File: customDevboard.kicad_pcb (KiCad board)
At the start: 2 copper layers, 39 x 39 mm, 83 parts, among them J1 USB_C_Receptacle_USB2.0_14P, J10 GPIO29_ADC3, J11 GND, J12 GPIO0, J13 GPIO1, J14 GPIO2, J15 GPIO3, J16 GPIO4, J17 GPIO5, J18 GPIO6, J19 GPIO7, J2 RUN, J20 GPIO8, J21 GPIO9, J22 Conn_01x01, J23 Conn_01x01, J24 Conn_01x01, J25 Conn_01x01, J26 Conn_01x01, J27 Conn_01x01, J28 Conn_01x01, J29 Conn_01x01, J3 3V3, J30 Conn_01x01, J31 Conn_01x01, J32 Conn_01x01, J33 Conn_01x01, J34 Conn_01x01, J35 Conn_01x01, J36 Conn_01x01, J37 Conn_01x01, J38 Conn_01x01, J39 Conn_01x01, J4 VBUS, J40 Conn_01x01, J41 Conn_01x01, J42 SWCLK, J43 GND, J44 SWD, J5 GND, J6 GND, J7 GPIO26_ADC0, J8 GPIO27_ADC1, J9 GPIO28_ADC2, SW1 BOOT, U1 RP2040, U2 W25Q128JVP, U3 TLV75733PDRV, Y1 12 MHz

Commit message: optimise more
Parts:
- moved C12 12.2 mm to (69.2, 69.0), turned to -90 degrees
- moved C11 10.8 mm to (70.2, 69.0), turned to -90 degrees
- moved C10 9.65 mm to (71.2, 69.0), turned to -90 degrees
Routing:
- net +1V1: track 39.9 -> 33.2 mm
- net GND: track 30.5 -> 26.5 mm
- net Net-(U1-USB_DM): track 10.5 -> 8.99 mm
- net Net-(U1-USB_DP): track 10.1 -> 8.97 mm

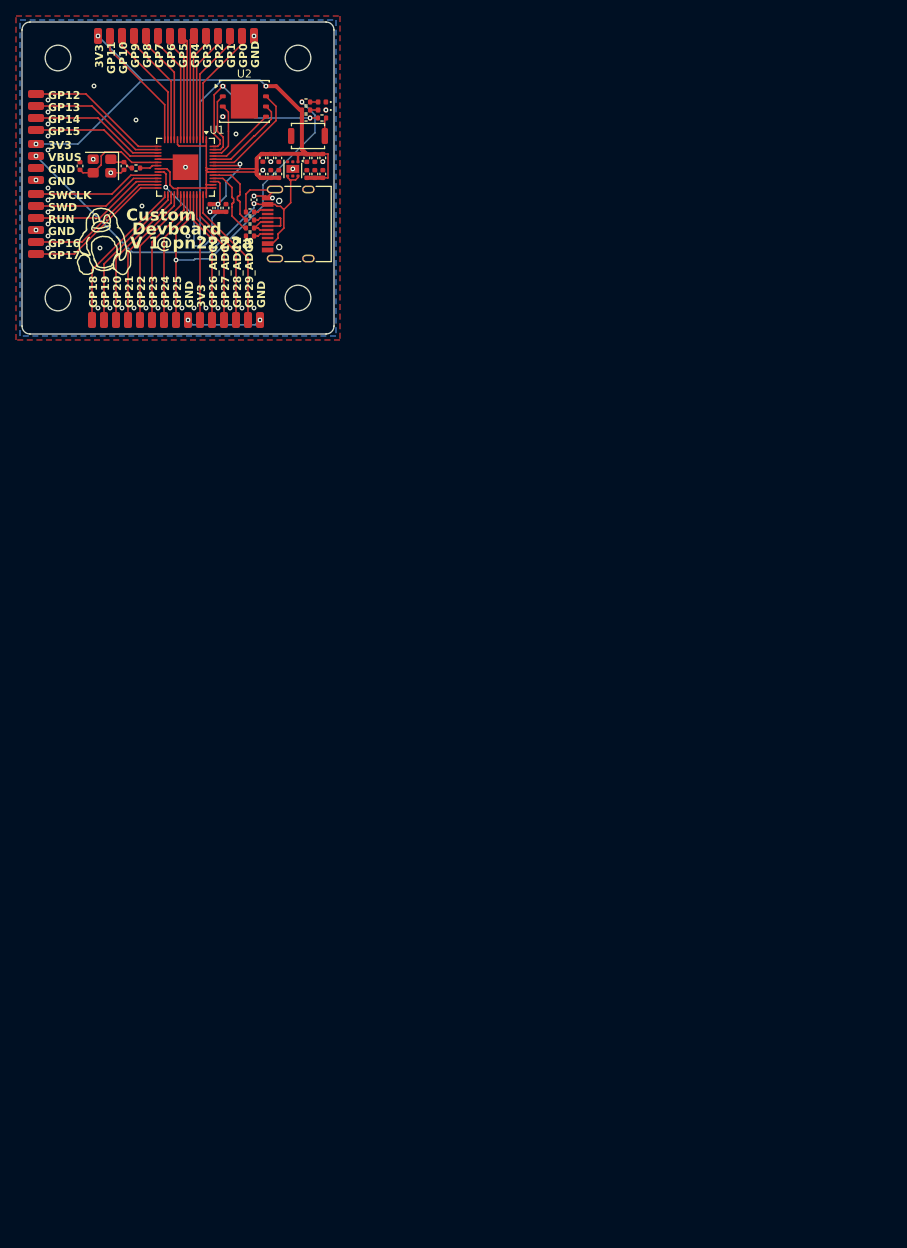
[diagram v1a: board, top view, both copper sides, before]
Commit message: switch to stm32
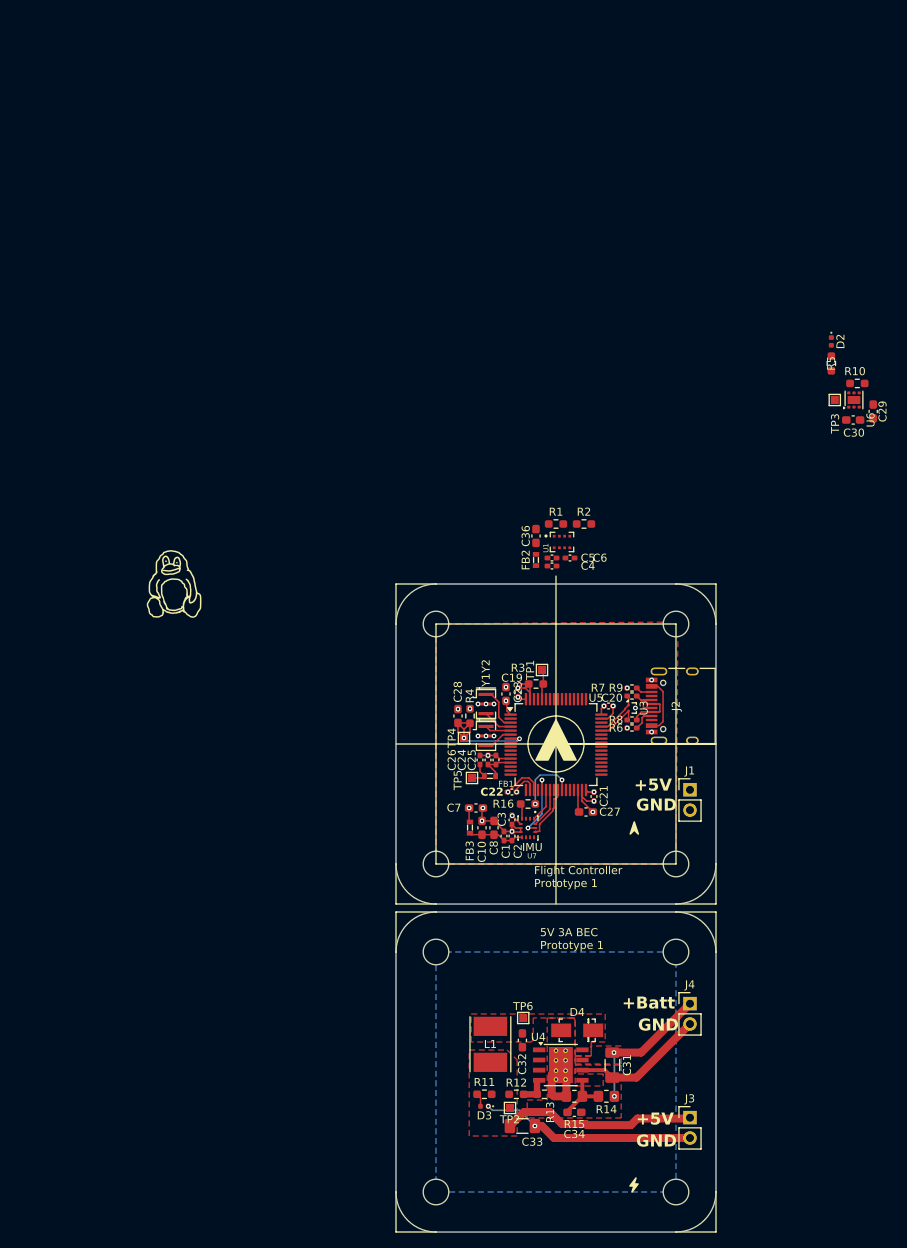
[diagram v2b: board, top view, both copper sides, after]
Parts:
- removed C11, C12, C17, C9: 0.1uF, Capacitor_SMD:C_0402_1005Metric
- removed C13, C18: 10uF, Capacitor_SMD:C_0402_1005Metric
- removed C14: 1uF, Capacitor_SMD:C_0402_1005Metric
- removed C15, C16: 33pF, Capacitor_SMD:C_0402_1005Metric
- removed D1: PWR_LED, LED_SMD:LED_0402_1005Metric
- removed J10: GPIO29_ADC3, Connector_Wire:SolderWirePad_1x01_SMD_1x2mm
- removed J11, J43, J5, J6: GND, Connector_Wire:SolderWirePad_1x01_SMD_1x2mm
- removed J12: GPIO0, Connector_Wire:SolderWirePad_1x01_SMD_1x2mm
- removed J13: GPIO1, Connector_Wire:SolderWirePad_1x01_SMD_1x2mm
- removed J14: GPIO2, Connector_Wire:SolderWirePad_1x01_SMD_1x2mm
- removed J15: GPIO3, Connector_Wire:SolderWirePad_1x01_SMD_1x2mm
- removed J16: GPIO4, Connector_Wire:SolderWirePad_1x01_SMD_1x2mm
- removed J17: GPIO5, Connector_Wire:SolderWirePad_1x01_SMD_1x2mm
- removed J18: GPIO6, Connector_Wire:SolderWirePad_1x01_SMD_1x2mm
- removed J19: GPIO7, Connector_Wire:SolderWirePad_1x01_SMD_1x2mm
- removed J20: GPIO8, Connector_Wire:SolderWirePad_1x01_SMD_1x2mm
- removed J21: GPIO9, Connector_Wire:SolderWirePad_1x01_SMD_1x2mm
- removed J22, J23, J24, J25, J26, J27, J28, J29, J30, J31, J32, J33, J34, J35, J36, J37, J38, J39, J40, J41: Conn_01x01, Connector_Wire:SolderWirePad_1x01_SMD_1x2mm
- removed J42: SWCLK, Connector_Wire:SolderWirePad_1x01_SMD_1x2mm
- removed J44: SWD, Connector_Wire:SolderWirePad_1x01_SMD_1x2mm
- removed J7: GPIO26_ADC0, Connector_Wire:SolderWirePad_1x01_SMD_1x2mm
- removed J8: GPIO27_ADC1, Connector_Wire:SolderWirePad_1x01_SMD_1x2mm
- removed J9: GPIO28_ADC2, Connector_Wire:SolderWirePad_1x01_SMD_1x2mm
- removed the REF** at (50.2, 80.2)
- removed the REF** at (80.2, 80.2)
- removed the REF** at (50.2, 50.2)
- removed the REF** at (80.2, 50.2)
- removed SW1: BOOT, Button_Switch_SMD:SW_Push_SPST_NO_Alps_SKRK
- removed U2: W25Q128JVP, Package_SON:WSON-8-1EP_6x5mm_P1.27mm_EP3.4x4.3mm
- added C19: 100nF, Capacitor_SMD:C_0402_1005Metric_Pad0.74x0.62mm_HandSolder, F.Cu at (107.8, 129.6)
- added C20: 100nF, Capacitor_SMD:C_0402_1005Metric_Pad0.74x0.62mm_HandSolder, F.Cu at (119.1, 131.2)
- added C21: 100nF, Capacitor_SMD:C_0402_1005Metric_Pad0.74x0.62mm_HandSolder, F.Cu at (117.2, 142.6)
- added C22: 100nF, Capacitor_SMD:C_0402_1005Metric_Pad0.74x0.62mm_HandSolder, F.Cu at (107.0, 142.0)
- added C23: 10uF, Capacitor_SMD:C_0603_1608Metric_Pad1.08x0.95mm_HandSolder, F.Cu at (106.2, 129.8)
- added C24: 10nF, Capacitor_SMD:C_0402_1005Metric_Pad0.74x0.62mm_HandSolder, F.Cu at (104.0, 138.0)
- added C25: 1uF, Capacitor_SMD:C_0402_1005Metric_Pad0.74x0.62mm_HandSolder, F.Cu at (105.0, 138.0)
- added C26: 1uF, Capacitor_SMD:C_0402_1005Metric_Pad0.74x0.62mm_HandSolder, F.Cu at (103.0, 138.0)
- added C27: 4.7uF, Capacitor_SMD:C_0603_1608Metric_Pad1.08x0.95mm_HandSolder, F.Cu at (116.2, 144.5)
- added C28: 100nF, Capacitor_SMD:C_0603_1608Metric_Pad1.08x0.95mm_HandSolder, F.Cu at (100.2, 132.5)
- added C29: 1uF, Capacitor_SMD:C_0603_1608Metric_Pad1.08x0.95mm_HandSolder, F.Cu at (152.2, 94.4)
- added C30: 2.2uF, Capacitor_SMD:C_0603_1608Metric_Pad1.08x0.95mm_HandSolder, F.Cu at (149.7, 95.5)
- added C31: 10uF, Capacitor_SMD:C_1206_3216Metric_Pad1.33x1.80mm_HandSolder, F.Cu at (119.5, 176.1)
- added C32: 10nF, Capacitor_SMD:C_0603_1608Metric_Pad1.08x0.95mm_HandSolder, F.Cu at (108.3, 173.0)
- added C33: 220uF, Capacitor_SMD:C_1206_3216Metric_Pad1.33x1.80mm_HandSolder, F.Cu at (108.3, 183.8)
- added C34: 10nF, Capacitor_SMD:C_0603_1608Metric_Pad1.08x0.95mm_HandSolder, F.Cu at (114.8, 182.0)
- added C36: 100nF, Capacitor_SMD:C_0603_1608Metric_Pad1.08x0.95mm_HandSolder, F.Cu at (110.0, 110.0)
- added D3: 5V LED, LED_SMD:LED_0402_1005Metric, F.Cu at (103.5, 181.3)
- added D4: B340A, digikey-footprints:DO-214AC, F.Cu at (115.2, 171.8)
- added FB1: BLM18PG121SN1D, digikey-footprints:0603, F.Cu at (104.2, 140.0)
- added FB2: BLM18AG601SN1D, digikey-footprints:0603, F.Cu at (110.0, 113.0)
- added FB3: BLM18AG601SN1D, digikey-footprints:0603, F.Cu at (101.8, 146.4)
- added L1: 18uH, Inductor_SMD:L_Taiyo-Yuden_NR-50xx_HandSoldering, F.Cu at (104.3, 173.5)
- added R10: 100k, Resistor_SMD:R_0603_1608Metric_Pad0.98x0.95mm_HandSolder, F.Cu at (150.2, 90.9)
- added R11: 10K, Resistor_SMD:R_0603_1608Metric_Pad0.98x0.95mm_HandSolder, F.Cu at (103.5, 179.8)
- added R12: 10k, Resistor_SMD:R_0603_1608Metric_Pad0.98x0.95mm_HandSolder, F.Cu at (107.5, 179.8)
- added R13: 3.24k, Resistor_SMD:R_0603_1608Metric_Pad0.98x0.95mm_HandSolder, F.Cu at (111.0, 179.8)
- added R14: 100k, Resistor_SMD:R_0805_2012Metric_Pad1.20x1.40mm_HandSolder, F.Cu at (118.8, 180.0)
- added R15: 18k, Resistor_SMD:R_0805_2012Metric_Pad1.20x1.40mm_HandSolder, F.Cu at (114.8, 180.0)
- added R16: 100, Resistor_SMD:R_0603_1608Metric_Pad0.98x0.95mm_HandSolder, F.Cu at (109.0, 143.5)
- added REF**: MountingHole_3.2mm_M3, MountingHole:MountingHole_3.2mm_M3, F.Cu at (127.5, 121.0)
- added REF**: MountingHole_3.2mm_M3, MountingHole:MountingHole_3.2mm_M3, F.Cu at (97.5, 162.0)
- added REF**: MountingHole_3.2mm_M3, MountingHole:MountingHole_3.2mm_M3, F.Cu at (97.5, 151.0)
- added REF**: MountingHole_3.2mm_M3, MountingHole:MountingHole_3.2mm_M3, F.Cu at (127.5, 192.0)
- added REF**: MountingHole_3.2mm_M3, MountingHole:MountingHole_3.2mm_M3, F.Cu at (97.5, 192.0)
- added REF**: MountingHole_3.2mm_M3, MountingHole:MountingHole_3.2mm_M3, F.Cu at (97.5, 121.0)
- added REF**: MountingHole_3.2mm_M3, MountingHole:MountingHole_3.2mm_M3, F.Cu at (127.5, 162.0)
- added REF**: MountingHole_3.2mm_M3, MountingHole:MountingHole_3.2mm_M3, F.Cu at (127.5, 151.0)
- added TP1: BOOT0, TestPoint:TestPoint_Pad_1.0x1.0mm, F.Cu at (110.8, 126.8)
- added TP2: +5V, TestPoint:TestPoint_Pad_1.0x1.0mm, F.Cu at (106.8, 181.5)
- added TP3: +3.3V, TestPoint:TestPoint_Pad_1.0x1.0mm, F.Cu at (147.3, 93.0)
- added TP4: NRST, TestPoint:TestPoint_Pad_1.0x1.0mm, F.Cu at (101.0, 135.2)
- added TP5: MCU VDDA, TestPoint:TestPoint_Pad_1.0x1.0mm, F.Cu at (102.0, 140.2)
- added TP6: Per datasheet, TestPoint:TestPoint_Pad_1.0x1.0mm, F.Cu at (108.4, 170.2)
- added U4: TPS5430DDA, Package_SO:TI_SO-PowerPAD-8_ThermalVias, F.Cu at (113.1, 176.1)
- added U5: STM32F722RET6, Package_QFP:LQFP-64_10x10mm_P0.5mm, F.Cu at (112.5, 136.1)
- added U6: TLV75733PDRV, Package_SON:WSON-6-1EP_2x2mm_P0.65mm_EP1x1.6mm, F.Cu at (149.8, 93.0)
- added U7: BMI270, BMI270:XDCR_BMI270, F.Cu at (109.0, 146.5)
- added Y2: 32.768KHz, Crystal:Resonator_SMD_Murata_CSTxExxV-3Pin_3.0x1.1mm, F.Cu at (103.8, 131.0)
- C1: value 1uF -> 100nF; footprint Capacitor_SMD:C_0402_1005Metric -> Capacitor_SMD:C_0402_1005Metric_Pad0.74x0.62mm_HandSolder
- C10: value 1uF -> 10uF; footprint Capacitor_SMD:C_0402_1005Metric -> Capacitor_SMD:C_0603_1608Metric_Pad1.08x0.95mm_HandSolder
- C2, C5: value 0.1uF -> 1uF; footprint Capacitor_SMD:C_0402_1005Metric -> Capacitor_SMD:C_0402_1005Metric_Pad0.74x0.62mm_HandSolder
- C3, C4, C6: value 0.1uF -> 100nF; footprint Capacitor_SMD:C_0402_1005Metric -> Capacitor_SMD:C_0402_1005Metric_Pad0.74x0.62mm_HandSolder
- C7, C8: value 0.1uF -> 100nF; footprint Capacitor_SMD:C_0402_1005Metric -> Capacitor_SMD:C_0603_1608Metric_Pad1.08x0.95mm_HandSolder
- D2: value USR_LED -> 3.3V LED
- J1: value USB_C_Receptacle_USB2.0_14P -> From BEC; footprint Connector_USB:USB_C_Receptacle_HRO_TYPE-C-31-M-12 -> Connector_PinHeader_2.54mm:PinHeader_1x02_P2.54mm_Vertical
- J2: value RUN -> USB_C_Receptacle_USB2.0_14P; footprint Connector_Wire:SolderWirePad_1x01_SMD_1x2mm -> Connector_USB:USB_C_Receptacle_HRO_TYPE-C-31-M-12
- J3: value 3V3 -> From BEC; footprint Connector_Wire:SolderWirePad_1x01_SMD_1x2mm -> Connector_PinHeader_2.54mm:PinHeader_1x02_P2.54mm_Vertical
- J4: value VBUS -> From Battery; footprint Connector_Wire:SolderWirePad_1x01_SMD_1x2mm -> Connector_PinHeader_2.54mm:PinHeader_1x02_P2.54mm_Vertical
- R1, R2: value 5.1K -> 4.7k; footprint Resistor_SMD:R_0402_1005Metric -> Resistor_SMD:R_0603_1608Metric_Pad0.98x0.95mm_HandSolder
- R3, R4: value 27 -> 10k; footprint Resistor_SMD:R_0402_1005Metric -> Resistor_SMD:R_0603_1608Metric_Pad0.98x0.95mm_HandSolder
- R5: value 1K -> 10K; footprint Resistor_SMD:R_0402_1005Metric -> Resistor_SMD:R_0603_1608Metric_Pad0.98x0.95mm_HandSolder
- R6: value 1K -> 5.1k; footprint Resistor_SMD:R_0402_1005Metric -> Resistor_SMD:R_0402_1005Metric_Pad0.72x0.64mm_HandSolder
- R7: value 10K -> 5.1k; footprint Resistor_SMD:R_0402_1005Metric -> Resistor_SMD:R_0402_1005Metric_Pad0.72x0.64mm_HandSolder
- R8, R9: value 1K -> 27; footprint Resistor_SMD:R_0402_1005Metric -> Resistor_SMD:R_0402_1005Metric_Pad0.72x0.64mm_HandSolder
- U1: value RP2040 -> DPS310; footprint Package_DFN_QFN:QFN-56-1EP_7x7mm_P0.4mm_EP3.2x3.2mm -> DPS310:XDCR_DPS310
- U3: value TLV75733PDRV -> TPD2EUSB30; footprint Package_SON:WSON-6-1EP_2x2mm_P0.65mm_EP1x1.6mm -> Package_TO_SOT_SMD:Texas_DRT-3
- Y1: value 12 MHz -> 8MHz; footprint Crystal:Crystal_SMD_3225-4Pin_3.2x2.5mm -> Crystal:Resonator_SMD_Murata_CSTxExxV-3Pin_3.0x1.1mm
- moved J3 146.6 mm to (129.2, 182.7), turned to 0 degrees
- moved J4 133.8 mm to (129.2, 168.5), turned to 0 degrees
- moved J2 101.4 mm to (128.5, 131.2), turned to 90 degrees
- moved R5 90.3 mm to (146.9, 88.4), turned to 90 degrees
- moved C1 89.3 mm to (106.0, 147.5), turned to 90 degrees
- moved R8 86.5 mm to (122.0, 133.0), turned to 180 degrees
- moved C3 86.3 mm to (107.0, 145.5)
- moved C2 86.1 mm to (107.0, 147.5)
- moved Y1 85.9 mm to (103.8, 135.0), turned to -90 degrees
- moved J1 85.9 mm to (129.2, 141.7), turned to 0 degrees
- moved R6 85.5 mm to (122.0, 134.0)
- moved C8 84.7 mm to (104.8, 146.5)
- moved R9 84.7 mm to (122.0, 130.0)
- moved C10 83.8 mm to (103.2, 146.5), turned to 90 degrees
- moved C7 83.5 mm to (102.5, 144.0), turned to 0 degrees
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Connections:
- C1 pad 1: +3V3 -> Net-(U7-VDD)
- C10 pad 1: +1V1 -> Net-(U7-VDD)
- C2 pad 1: +3V3 -> Net-(U7-VDD)
- C3 pad 1: +3V3 -> +3.3V
- C4 pad 1: +3V3 -> Net-(U1-VDD)
- C5 pad 1: +3V3 -> Net-(U1-VDD)
- C6 pad 1: +3V3 -> +3.3V
- C7 pad 1: +3V3 -> +3.3V
- C8 pad 1: +3V3 -> Net-(U7-VDD)
- J3 pad 1: +3V3 -> +5V
- J4 pad 1: VBUS -> +BATT
- R1 pad 1: Net-(J1-CC1) -> Net-(U1-VDD)
- R1 pad 2: GND -> I2C1_SDA
- R2 pad 1: GND -> Net-(U1-VDD)
- R2 pad 2: Net-(J1-CC2) -> I2C1_SCL
- R3 pad 1: USB_D+ -> Net-(U5-BOOT0)
- R3 pad 2: Net-(U1-USB_DP) -> GND
- R4 pad 1: USB_D- -> +3.3V
- R4 pad 2: Net-(U1-USB_DM) -> Net-(U5-NRST)
- R5 pad 1: Net-(C16-Pad2) -> +3.3V
- R5 pad 2: XOUT -> Net-(D2-A)
- R6 pad 1: Net-(R6-Pad1) -> Net-(J2-CC1)
- R6 pad 2: QSPI_SS -> GND
- R7 pad 1: QSPI_SS -> GND
- R7 pad 2: +3V3 -> Net-(J2-CC2)
- R8 pad 1: +3V3 -> Net-(J2-D--PadA7)
- R8 pad 2: Net-(D1-A) -> USB_D-
- R9 pad 1: GPIO25 -> USB_D+
- R9 pad 2: Net-(D2-A) -> Net-(J2-D+-PadA6)
- U1 pad 1: +3V3 -> GND
- U1 pad 2: GPIO0 -> +3.3V
- U1 pad 3: GPIO1 -> I2C1_SDA
- U1 pad 4: GPIO2 -> I2C1_SCL
- U1 pad 5: GPIO3 -> GND
- U1 pad 6: GPIO4 -> +3.3V
- U1 pad 7: GPIO5 -> GND
- U1 pad 8: GPIO6 -> Net-(U1-VDD)
- U3 pad 1: +3V3 -> USB_D+
- U3 pad 2: unconnected-(U3-NC-Pad2) -> USB_D-
- Y1 pad 1: Net-(C16-Pad2) -> Net-(U5-PH0)
- Y1 pad 3: XIN -> Net-(U5-PH1)
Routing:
- net +3V3: track 138.1 -> 0.00 mm, vias 4 -> 0
- net GND: track 26.5 -> 86.1 mm, vias 48 -> 24
- net GPIO25: track 46.4 -> 0.00 mm, vias 2 -> 0
- net VBUS: track 50.0 -> 7.08 mm, vias 2 -> 0
- net +1V1: track 33.2 -> 0.00 mm, vias 3 -> 0
- net +5V: track 0.00 -> 24.3 mm
- net QSPI_SS: track 22.5 -> 0.00 mm, vias 2 -> 0
- net GPIO18: track 19.4 -> 0.00 mm
- net GPIO19: track 19.0 -> 0.00 mm
- net GPIO17: track 18.7 -> 0.00 mm
- net GPIO20: track 18.5 -> 0.00 mm
- net GPIO16: track 18.2 -> 0.00 mm
- net GPIO21: track 18.1 -> 0.00 mm
- net GPIO29_ADC3: track 18.0 -> 0.00 mm
- net GPIO12: track 18.0 -> 0.00 mm
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- added copper zone on In1.Cu, net +3.3V
- added copper zone on F.Cu, net +5V
- added copper zone on F.Cu, net +BATT
- added copper zone on In2.Cu, net GND
- added copper zone on F.Cu, net Net-(U4-PH)
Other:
- board size 39 x 39 mm -> 40 x 81 mm
- copper layers 2 -> 4
- board text added: "+5V"
- board text added: "+Batt"
- board text added: "5V 3A BEC Prototype 1"
- board text added: "Flight Controller Prototype 1"
- board text added: "IMU"
- board text removed: "3V3"
- board text removed: "@pn2222a"
- board text removed: "Custom"
- board text removed: "Devboard"
- board text removed: "GP0"
- board text removed: "GP1"
- board text removed: "GP10"
- board text removed: "GP11"
- board text removed: "GP12"
- board text removed: "GP13"
- board text removed: "GP14"
- board text removed: "GP15"
- board text removed: "GP16"
- board text removed: "GP17"
- board text removed: "GP18"
- board text removed: "GP19"
- board text removed: "GP2"
- board text removed: "GP20"
- board text removed: "GP21"
- board text removed: "GP22"
- board text removed: "GP23"
- board text removed: "GP24"
- board text removed: "GP25"
- board text removed: "GP26_ADC0"
- board text removed: "GP27_ADC1"
- board text removed: "GP28_ADC2"
- board text removed: "GP29_ADC3"
- board text removed: "GP3"
- board text removed: "GP4"
- board text removed: "GP5"
- board text removed: "GP6"
- board text removed: "GP7"
- board text removed: "GP8"
- board text removed: "GP9"
- board text removed: "RUN"
- board text removed: "SWCLK"
- board text removed: "SWD"
- board text removed: "V 1"
- board text removed: "VBUS"
